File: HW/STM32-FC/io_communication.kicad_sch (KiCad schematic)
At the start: 17 parts, among them J12 GH 1.25mm 6P, J13 GH 1.25mm 6P, J14 GH 1.25mm 4P, J15 GH 1.25mm 4P, J16 GH 1.25mm 4P, U12 ATA6561-GBQW, U13 ATA6561-GBQW

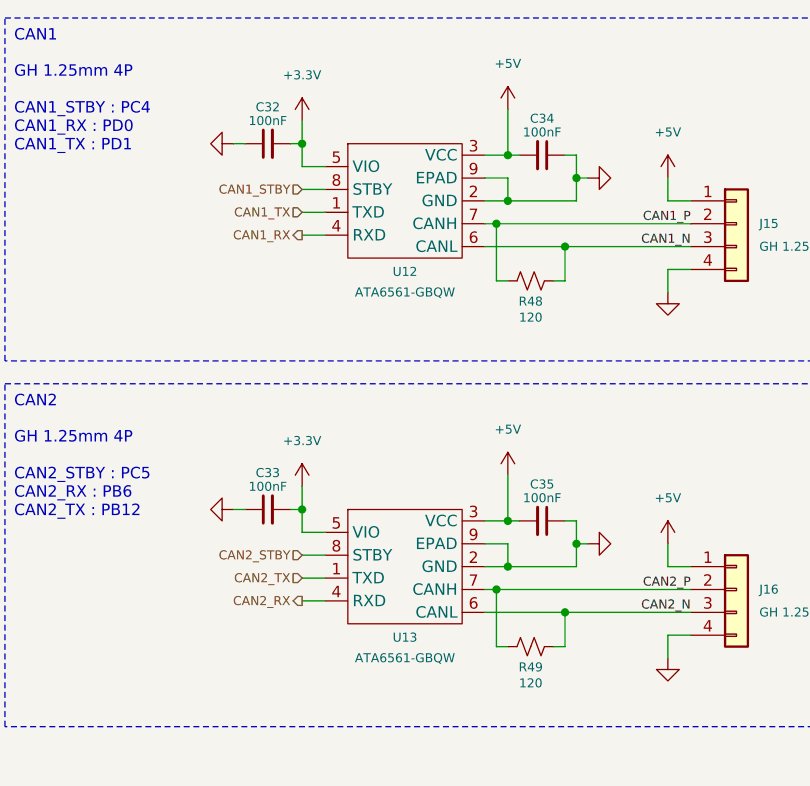
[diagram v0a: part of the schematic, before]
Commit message: HW Lib and RC code refactoring, GCS_log united and BMI323 IMU init.
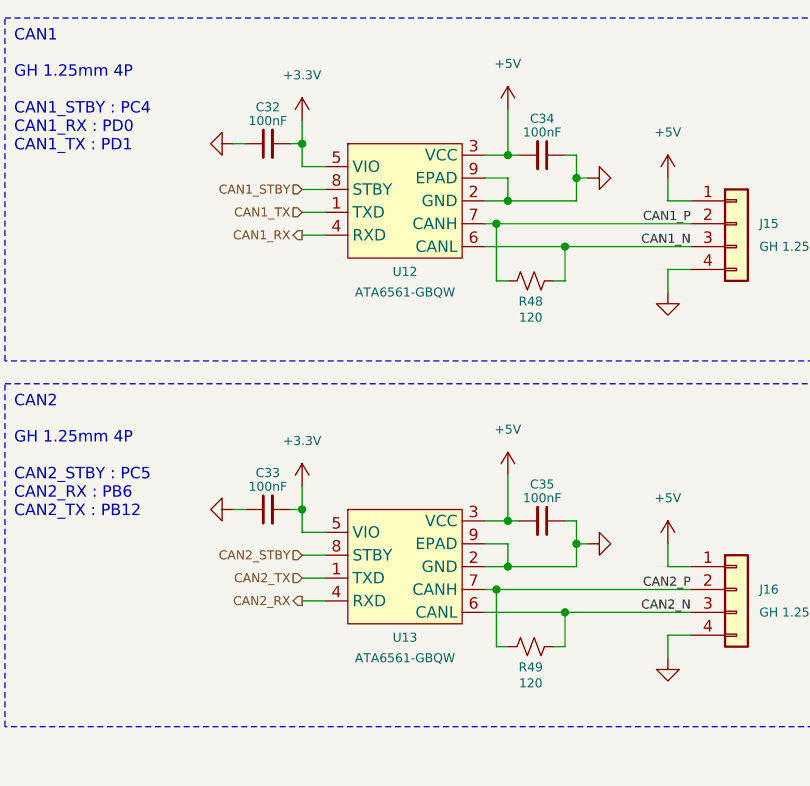
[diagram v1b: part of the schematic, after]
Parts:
- U12, U13: symbol ATA6561-GBQW:ATA6561-GBQW_2 -> ATA6561-GBQW:ATA6561-GBQW_Small
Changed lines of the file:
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@@
 	(title_block
 		(title "Communication")
-		(date "2025-04-13")
+		(date "2025-06-19")
 		(rev "A")
 		(company "NARAE")
@@
 	)
 	(symbol
-		(lib_id "ATA6561-GBQW:ATA6561-GBQW_2")
+		(lib_id "ATA6561-GBQW:ATA6561-GBQW_Small")
 		(at 133.35 33.02 0)
 		(unit 1)
@@
 			)
 		)
-		(property "Datasheet" "ATA6561-GAQW"
+		(property "Datasheet" "kicad-embed://ATA6561-GBQW.pdf"
 			(at 132.08 39.37 0)
 			(effects
@@
 			)
 		)
-		(property "Description" ""
+		(property "Description" "High-Speed CAN Transceiver with Standby Mode CAN FD Ready, 8-Lead VDFN"
 			(at 132.08 39.37 0)
 			(effects
@@
 	)
 	(symbol
-		(lib_id "ATA6561-GBQW:ATA6561-GBQW_2")
+		(lib_id "ATA6561-GBQW:ATA6561-GBQW_Small")
 		(at 133.35 73.66 0)
 		(unit 1)
@@
 			)
 		)
-		(property "Datasheet" "ATA6561-GAQW"
+		(property "Datasheet" "kicad-embed://ATA6561-GBQW.pdf"
 			(at 132.08 80.01 0)
 			(effects
@@
 			)
 		)
-		(property "Description" ""
+		(property "Description" "High-Speed CAN Transceiver with Standby Mode CAN FD Ready, 8-Lead VDFN"
 			(at 132.08 80.01 0)
 			(effects
